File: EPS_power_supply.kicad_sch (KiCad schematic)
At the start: 15 parts, among them IC1 TPS7B8733QDDARQ1, IC2 TPS7B8750QDDARQ1

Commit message: Big final PCU PCB design
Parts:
- added R_BYPASS1, R_BYPASS16: 0, Resistor_SMD:R_0603_1608Metric, symbol Device:R
- added TP1: 3V3_rail, TestPoint:TestPoint_Pad_D2.0mm, symbol Connector:TestPoint_Probe
- added TP2_3V_preOR1: ~, TestPoint:TestPoint_Pad_D2.0mm, symbol Connector:TestPoint_Probe
- added TP34: GND, TestPoint:TestPoint_Pad_D2.0mm, symbol Connector:TestPoint_Probe
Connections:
- net 3V3: now also R_BYPASS16.2, TP1.1
- net 3V3_LDO: now also TP2_3V_preOR1.1
- net 3V3_PDU: now also R_BYPASS16.1
- net 5V: now also R_BYPASS1.2
- net 5V_LDO: now also R_BYPASS1.1
- net GND: now also TP34.1
- no-connect marks 0 -> 4
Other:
- moved on the sheet: D5, D6, D7

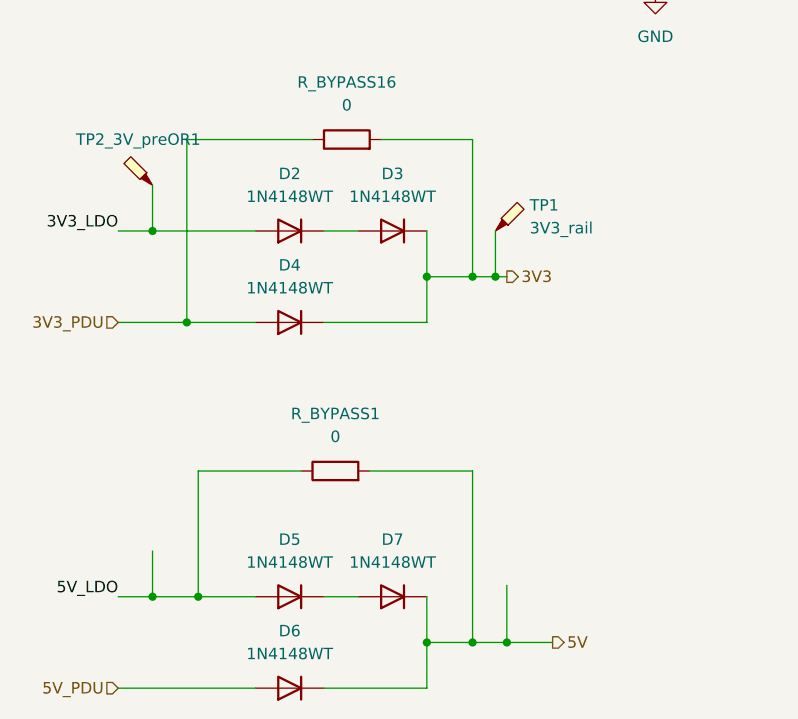
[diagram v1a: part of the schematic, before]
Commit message: Replaced Oring simple diodes with schottky
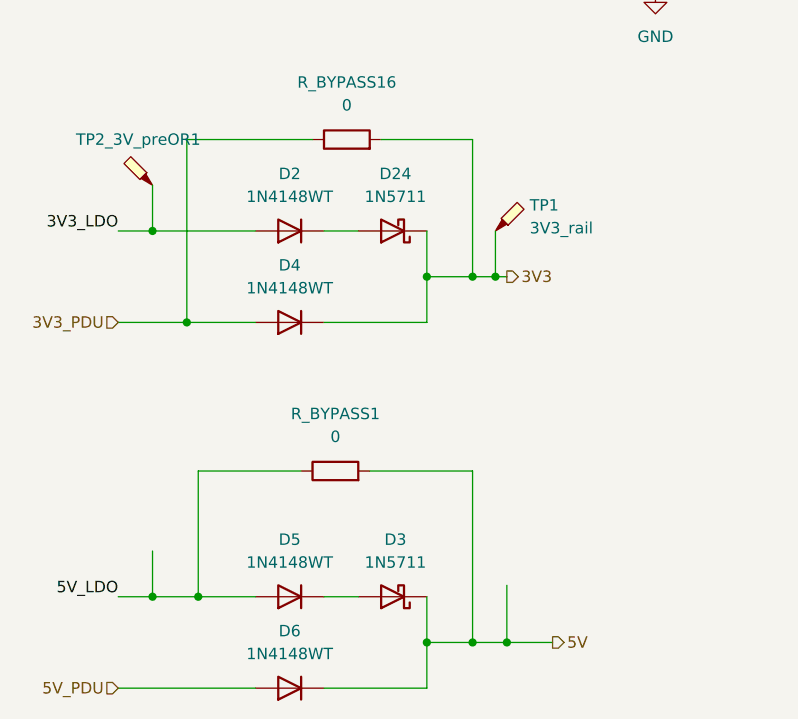
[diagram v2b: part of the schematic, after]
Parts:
- removed D3, D7: 1N4148WT, Diode_SMD:D_SOD-523, symbol Diode:1N4148WT
- added D24, D3: 1N5711, Diode_THT:D_DO-35_SOD27_P7.62mm_Horizontal, symbol Diode:1N5711
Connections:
- net 3V3: now also D24.1 (K)
- net 5V: now also D3.1 (K)
- net at D5.1 (K): now also D3.2 (A)
- net at D2.1 (K): now also D24.2 (A)
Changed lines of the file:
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@@
+	)
+	(symbol
+		(lib_id "Diode:1N5711")
+		(at 68.58 104.14 180)
+		(unit 1)
+		(exclude_from_sim no)
+		(in_bom yes)
+		(on_board yes)
+		(dnp no)
+		(fields_autoplaced yes)
+		(property "Reference" "D24"
+			(at 68.8975 97.79 0)
+			(effects
+				(font
+					(size 1.27 1.27)
+				)
+			)
+		)
+		(property "Value" "1N5711"
+			(at 68.8975 100.33 0)
+			(effects
+				(font
+					(size 1.27 1.27)
+				)
+			)
+		)
+		(property "Footprint" "Diode_THT:D_DO-35_SOD27_P7.62mm_Horizontal"
+			(at 68.58 99.695 0)
+			(effects
+				(font
+					(size 1.27 1.27)
+				)
+				(hide yes)
+			)
+		)
+		(property "Datasheet" "https://www.microsemi.com/document-portal/doc_download/8865-lds-0040-datasheet"
+			(at 68.58 104.14 0)
+			(effects
+				(font
+					(size 1.27 1.27)
+				)
+				(hide yes)
+			)
+		)
+		(property "Description" "70V 33mA Schottky diode, DO-35"
+			(at 68.58 104.14 0)
+			(effects
+				(font
+					(size 1.27 1.27)
+				)
+				(hide yes)
+			)
+		)
+		(pin "1"
+		)
+		(pin "2"
+		)
+		(instances
+			(project ""
+				(path "/2de881bb-2e2a-47f9-96ed-b3393fa36b98/8bf4b950-7d1e-4a2d-ad03-078c0e232a33"
+					(reference "D24")
+					(unit 1)
+				)
+			)
+		)
 	)
 	(symbol
@@
 				(path "/2de881bb-2e2a-47f9-96ed-b3393fa36b98/8bf4b950-7d1e-4a2d-ad03-078c0e232a33"
 					(reference "TP34")
+					(unit 1)
+				)
+			)
+		)
+	)
+	(symbol
+		(lib_id "Diode:1N5711")
+		(at 68.58 144.78 180)
+		(unit 1)
+		(exclude_from_sim no)
+		(in_bom yes)
+		(on_board yes)
+		(dnp no)
+		(fields_autoplaced yes)
+		(property "Reference" "D3"
+			(at 68.8975 138.43 0)
+			(effects
+				(font
+					(size 1.27 1.27)
+				)
+			)
+		)
+		(property "Value" "1N5711"
+			(at 68.8975 140.97 0)
+			(effects
+				(font
+					(size 1.27 1.27)
+				)
+			)
+		)
+		(property "Footprint" "Diode_THT:D_DO-35_SOD27_P7.62mm_Horizontal"
+			(at 68.58 140.335 0)
+			(effects
+				(font
+					(size 1.27 1.27)
+				)
+				(hide yes)
+			)
+		)
+		(property "Datasheet" "https://www.microsemi.com/document-portal/doc_download/8865-lds-0040-datasheet"
+			(at 68.58 144.78 0)
+			(effects
+				(font
+					(size 1.27 1.27)
+				)
+				(hide yes)
+			)
+		)
+		(property "Description" "70V 33mA Schottky diode, DO-35"
+			(at 68.58 144.78 0)
+			(effects
+				(font
+					(size 1.27 1.27)
+				)
+				(hide yes)
+			)
+		)
+		(pin "1"
+		)
+		(pin "2"
+		)
+		(instances
+			(project "PULSE_ENG"
+				(path "/2de881bb-2e2a-47f9-96ed-b3393fa36b98/8bf4b950-7d1e-4a2d-ad03-078c0e232a33"
+					(reference "D3")
 					(unit 1)
 				)
@@
 	)
 	(symbol
-		(lib_id "Diode:1N4148WT")
-		(at 68.58 104.14 180)
-		(unit 1)
-		(exclude_from_sim no)
-		(in_bom yes)
-		(on_board yes)
-		(dnp no)
-		(fields_autoplaced yes)
-		(property "Reference" "D3"
-			(at 68.58 97.79 0)
-			(effects
-				(font
-					(size 1.27 1.27)
-				)
-			)
-		)
-		(property "Value" "1N4148WT"
-			(at 68.58 100.33 0)
-			(effects
-				(font
-					(size 1.27 1.27)
-				)
-			)
-		)
-		(property "Footprint" "Diode_SMD:D_SOD-523"
-			(at 68.58 99.695 0)
-			(effects
-				(font
-					(size 1.27 1.27)
-				)
-				(hide yes)
-			)
-		)
-		(property "Datasheet" "https://www.diodes.com/assets/Datasheets/ds30396.pdf"
-			(at 68.58 104.14 0)
-			(effects
-				(font
-					(size 1.27 1.27)
-				)
-				(hide yes)
-			)
-		)
-		(property "Description" "75V 0.15A Fast switching Diode, SOD-523"
-			(at 68.58 104.14 0)
-			(effects
-				(font
-					(size 1.27 1.27)
-				)
-				(hide yes)
-			)
-		)
-		(property "Sim.Device" "D"
-			(at 68.58 104.14 0)
-			(effects
-				(font
-					(size 1.27 1.27)
-				)
-				(hide yes)
-			)
-		)
-		(property "Sim.Pins" "1=K 2=A"
-			(at 68.58 104.14 0)
-			(effects
-				(font
-					(size 1.27 1.27)
-				)
-				(hide yes)
-			)
-		)
-		(pin "1"
-		)
-		(pin "2"
-		)
-		(instances
-			(project "PULSE_ENG"
-				(path "/2de881bb-2e2a-47f9-96ed-b3393fa36b98/8bf4b950-7d1e-4a2d-ad03-078c0e232a33"
-					(reference "D3")
-					(unit 1)
-				)
-			)
-		)
-	)
-	(symbol
 		(lib_id "Device:C_Small")
 		(at 214.63 110.49 0)
@@
 					(unit 1)
 				)
-			)
-		)
-	)
-	(symbol
-		(lib_id "Diode:1N4148WT")
-		(at 68.58 144.78 180)
-		(unit 1)
-		(exclude_from_sim no)
-		(in_bom yes)
-		(on_board yes)
-		(dnp no)
-		(fields_autoplaced yes)
-		(property "Reference" "D7"
-			(at 68.58 138.43 0)
-			(effects
-				(font
-					(size 1.27 1.27)
-				)
-			)
-		)
-		(property "Value" "1N4148WT"
-			(at 68.58 140.97 0)
-			(effects
-				(font
-					(size 1.27 1.27)
-				)
-			)
-		)
-		(property "Footprint" "Diode_SMD:D_SOD-523"
-			(at 68.58 140.335 0)
-			(effects
-				(font
-					(size 1.27 1.27)
-				)
-				(hide yes)
-			)
-		)
-		(property "Datasheet" "https://www.diodes.com/assets/Datasheets/ds30396.pdf"
-			(at 68.58 144.78 0)
-			(effects
-				(font
-					(size 1.27 1.27)
-				)
-				(hide yes)
-			)
-		)
-		(property "Description" "75V 0.15A Fast switching Diode, SOD-523"
-			(at 68.58 144.78 0)
-			(effects
-				(font
-					(size 1.27 1.27)
-				)
-				(hide yes)
-			)
-		)
-		(property "Sim.Device" "D"
-			(at 68.58 144.78 0)
-			(effects
-				(font
-					(size 1.27 1.27)
-				)
-				(hide yes)
-			)
-		)
-		(property "Sim.Pins" "1=K 2=A"
-			(at 68.58 144.78 0)
-			(effects
-				(font
-					(size 1.27 1.27)
-				)
-				(hide yes)
-			)
-		)
-		(pin "1"
-		)
-		(pin "2"
-		)
-		(instances
-			(project "PULSE_ENG"
-				(path "/2de881bb-2e2a-47f9-96ed-b3393fa36b98/8bf4b950-7d1e-4a2d-ad03-078c0e232a33"
-					(reference "D7")
-					(unit 1)
-				)
